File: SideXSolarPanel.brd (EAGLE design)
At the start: 81.7 x 102 mm, 33 parts

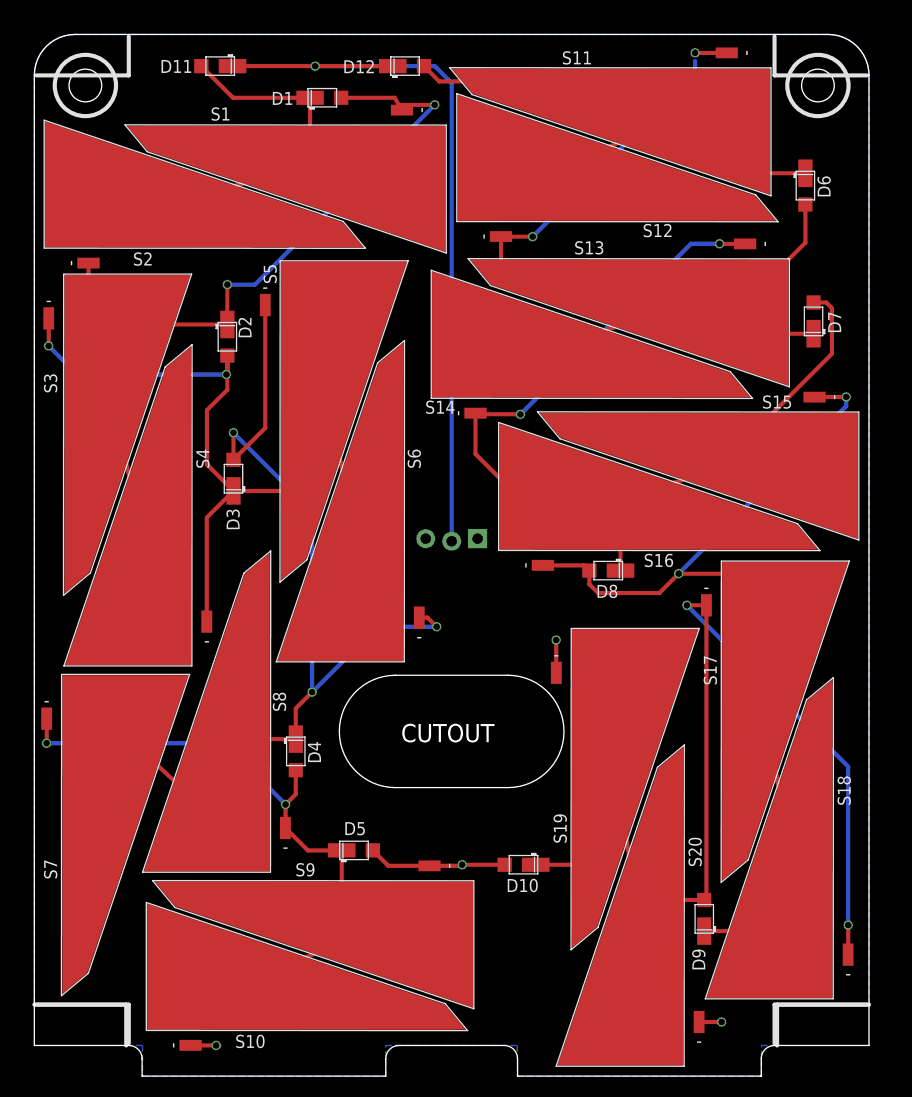
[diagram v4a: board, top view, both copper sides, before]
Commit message: Increased cutout line width
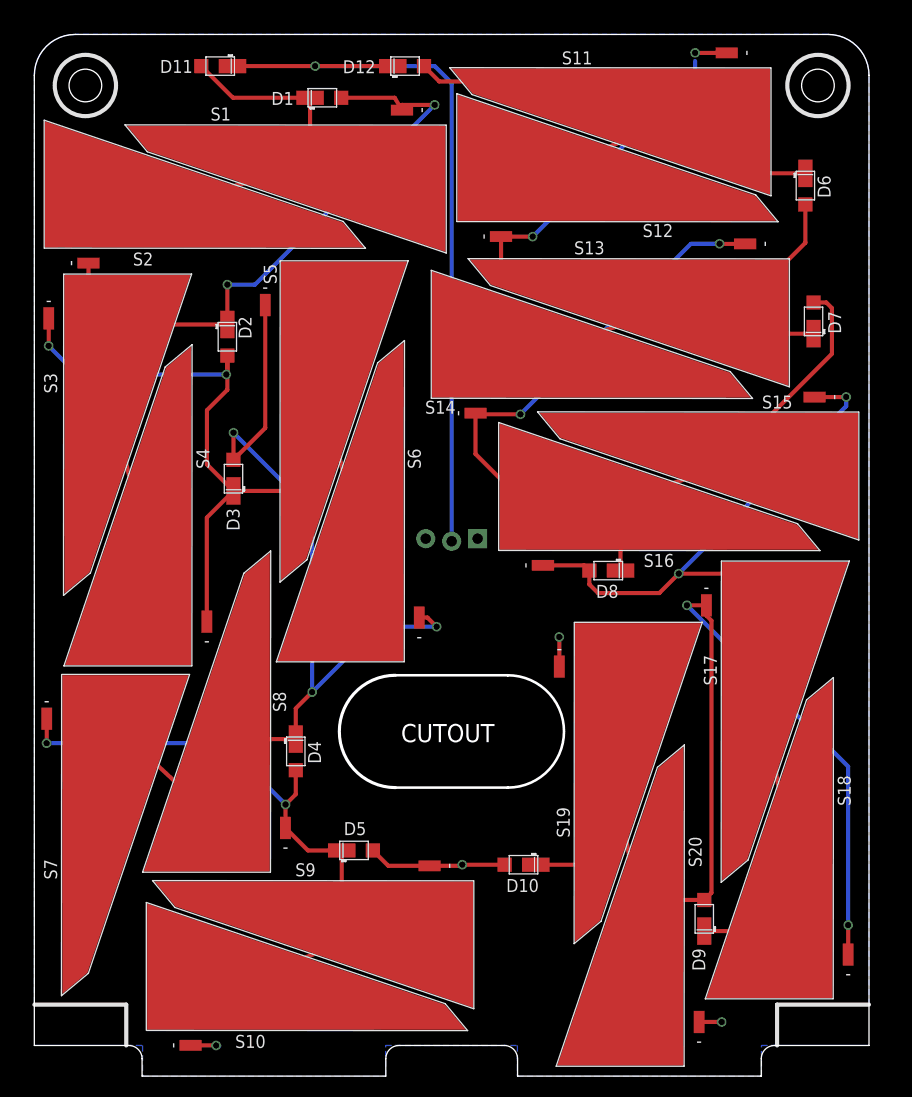
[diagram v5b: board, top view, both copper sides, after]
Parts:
- moved S19 0.67 mm to (53.0, 34.1)
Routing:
- net N$41: track 127.3 -> 128.2 mm
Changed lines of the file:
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@@
 <layer number="42" name="bRestrict" color="1" fill="10" visible="no" active="yes"/>
 <layer number="43" name="vRestrict" color="2" fill="10" visible="no" active="yes"/>
-<layer number="44" name="Drills" color="7" fill="1" visible="yes" active="yes"/>
-<layer number="45" name="Holes" color="7" fill="1" visible="yes" active="yes"/>
+<layer number="44" name="Drills" color="7" fill="1" visible="no" active="yes"/>
+<layer number="45" name="Holes" color="7" fill="1" visible="no" active="yes"/>
 <layer number="46" name="Milling" color="3" fill="1" visible="no" active="yes"/>
 <layer number="47" name="Measures" color="7" fill="1" visible="no" active="yes"/>
@@
 <wire x1="46.015" y1="0" x2="47.315" y2="-1.3" width="0" layer="20" curve="-90"/>
 <wire x1="71.18" y1="-1.3" x2="72.48" y2="0" width="0" layer="20" curve="-90"/>
-<wire x1="0.2" y1="4" x2="9.25" y2="4" width="0.4" layer="121"/>
-<wire x1="9.25" y1="4" x2="9.25" y2="0.2" width="0.4" layer="121"/>
-<wire x1="81.53" y1="94.99" x2="72.48" y2="94.99" width="0.4" layer="121"/>
-<wire x1="72.48" y1="94.99" x2="72.48" y2="98.79" width="0.4" layer="121"/>
-<wire x1="0.2" y1="94.99" x2="9.25" y2="94.99" width="0.4" layer="121"/>
-<wire x1="9.25" y1="94.99" x2="9.25" y2="98.79" width="0.4" layer="121"/>
-<wire x1="81.53" y1="4" x2="72.48" y2="4" width="0.4" layer="121"/>
-<wire x1="72.48" y1="4" x2="72.48" y2="0.2" width="0.4" layer="121"/>
-<rectangle x1="13.1" y1="58.8" x2="28.9" y2="77.8" layer="122"/>
 <hole x="5" y="94" drill="3.2"/>
 <hole x="76.73" y="94" drill="3.2"/>
-<wire x1="35.365" y1="25.25" x2="46.365" y2="25.25" width="0" layer="20"/>
-<wire x1="35.365" y1="36.25" x2="46.365" y2="36.25" width="0" layer="20"/>
-<wire x1="35.365" y1="36.25" x2="35.365" y2="25.25" width="0" layer="20" curve="180"/>
-<wire x1="46.365" y1="25.25" x2="46.365" y2="36.25" width="0" layer="20" curve="180"/>
+<wire x1="35.365" y1="25.25" x2="46.365" y2="25.25" width="0.254" layer="20"/>
+<wire x1="35.365" y1="36.25" x2="46.365" y2="36.25" width="0.254" layer="20"/>
+<wire x1="35.365" y1="36.25" x2="35.365" y2="25.25" width="0.3048" layer="20" curve="180"/>
+<wire x1="46.365" y1="25.25" x2="46.365" y2="36.25" width="0.254" layer="20" curve="180"/>
 <text x="35.9" y="29.7" size="1.778" layer="20">CUTOUT</text>
 <wire x1="0" y1="4" x2="9" y2="4" width="0.4064" layer="21"/>
@@
 <attribute name="NAME" x="9.65" y="76.37" size="1.27" layer="25"/>
 </element>
-<element name="S19" library="phonesat" package="SOLAR_CELL" value="SOLAR_CELL" x="52.7" y="33.5" smashed="yes">
-<attribute name="NAME" x="52.13" y="19.75" size="1.27" layer="25" rot="R90"/>
+<element name="S19" library="phonesat" package="SOLAR_CELL" value="SOLAR_CELL" x="53" y="34.1" smashed="yes">
+<attribute name="NAME" x="52.43" y="20.35" size="1.27" layer="25" rot="R90"/>
 </element>
 <element name="S20" library="phonesat" package="SOLAR_CELL" value="SOLAR_CELL" x="63.5" y="5.3" smashed="yes" rot="R180">
@@
 <wire x1="67.3" y1="2.3" x2="67.4" y2="2.3" width="0.4064" layer="16"/>
 <wire x1="67.4" y1="2.3" x2="67.4" y2="2.2" width="0.4064" layer="16"/>
-<wire x1="51.1107" y1="36.4991" x2="51.1" y2="36.4991" width="0.4064" layer="1"/>
-<wire x1="51.1" y1="36.4991" x2="51.1" y2="39.7" width="0.4064" layer="1"/>
-<via x="51.1" y="39.7" extent="1-16" drill="0.6"/>
-<wire x1="51.1" y1="39.7" x2="51.2" y2="39.7" width="0.4064" layer="16"/>
+<wire x1="51.4107" y1="37.0991" x2="51.1" y2="36.4991" width="0.4064" layer="1"/>
 <wire x1="38.6991" y1="17.5893" x2="34.6607" y2="17.5893" width="0.4064" layer="1"/>
 <wire x1="34.6607" y1="17.5893" x2="33.15" y2="19.1" width="0.4064" layer="1"/>
 <wire x1="46.05" y1="17.7" x2="41.9" y2="17.7" width="0.4064" layer="1"/>
+<wire x1="51.4107" y1="37.0991" x2="51.4107" y2="39.9893" width="0.4064" layer="1"/>
+<wire x1="51.4107" y1="39.9893" x2="51.4" y2="40" width="0.4064" layer="1"/>
+<via x="51.4" y="40" extent="1-16" drill="0.6"/>
+<wire x1="51.4" y1="40" x2="51.3" y2="40.1" width="0.4064" layer="16"/>
+<wire x1="51.3" y1="40.1" x2="43.405" y2="49.627" width="0" layer="19" extent="1-16"/>
 </signal>
 <signal name="N$36">
@@
 <contactref element="S17" pad="1"/>
 <contactref element="S19" pad="2"/>
-<wire x1="54.8874" y1="38.5114" x2="57.72385625" y2="21.63763125" width="0.4064" layer="1"/>
+<wire x1="55.1874" y1="39.1114" x2="57.72385625" y2="21.63763125" width="0.4064" layer="1"/>
 <wire x1="57.72385625" y1="21.63763125" x2="58.9777125" y2="14.178584375" width="0.4064" layer="1"/>
 <wire x1="58.9777125" y1="14.178584375" x2="61.3126" y2="0.2886" width="0.4064" layer="1"/>
@@
 <wire x1="65.6" y1="14.25" x2="59.049128125" y2="14.25" width="0.4064" layer="1"/>
 <wire x1="59.049128125" y1="14.25" x2="58.9777125" y2="14.178584375" width="0.4064" layer="1"/>
-<wire x1="65.8107" y1="43.0991" x2="65.8107" y2="14.4607" width="0.4064" layer="1"/>
-<wire x1="65.8107" y1="14.4607" x2="65.6" y2="14.25" width="0.4064" layer="1"/>
 <wire x1="79.6893" y1="8.9009" x2="79.6893" y2="11.7893" width="0.4064" layer="1"/>
 <wire x1="79.6893" y1="11.7893" x2="79.7" y2="11.8" width="0.4064" layer="1"/>
@@
 <wire x1="63.9" y1="43.1" x2="65.8098" y2="43.1" width="0.4064" layer="1"/>
 <wire x1="65.8098" y1="43.1" x2="65.8107" y2="43.0991" width="0.4064" layer="1"/>
+<wire x1="65.6" y1="14.25" x2="66.3" y2="14.95" width="0.4064" layer="1"/>
+<wire x1="66.3" y1="14.95" x2="66.3" y2="41.6" width="0.4064" layer="1"/>
+<wire x1="66.3" y1="41.6" x2="65.8107" y2="42.0893" width="0.4064" layer="1"/>
+<wire x1="65.8107" y1="42.0893" x2="65.8107" y2="43.0991" width="0.4064" layer="1"/>
 </signal>
 <signal name="N$45">

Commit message: Swapped X and Y solar panels per NanoRacks ICD
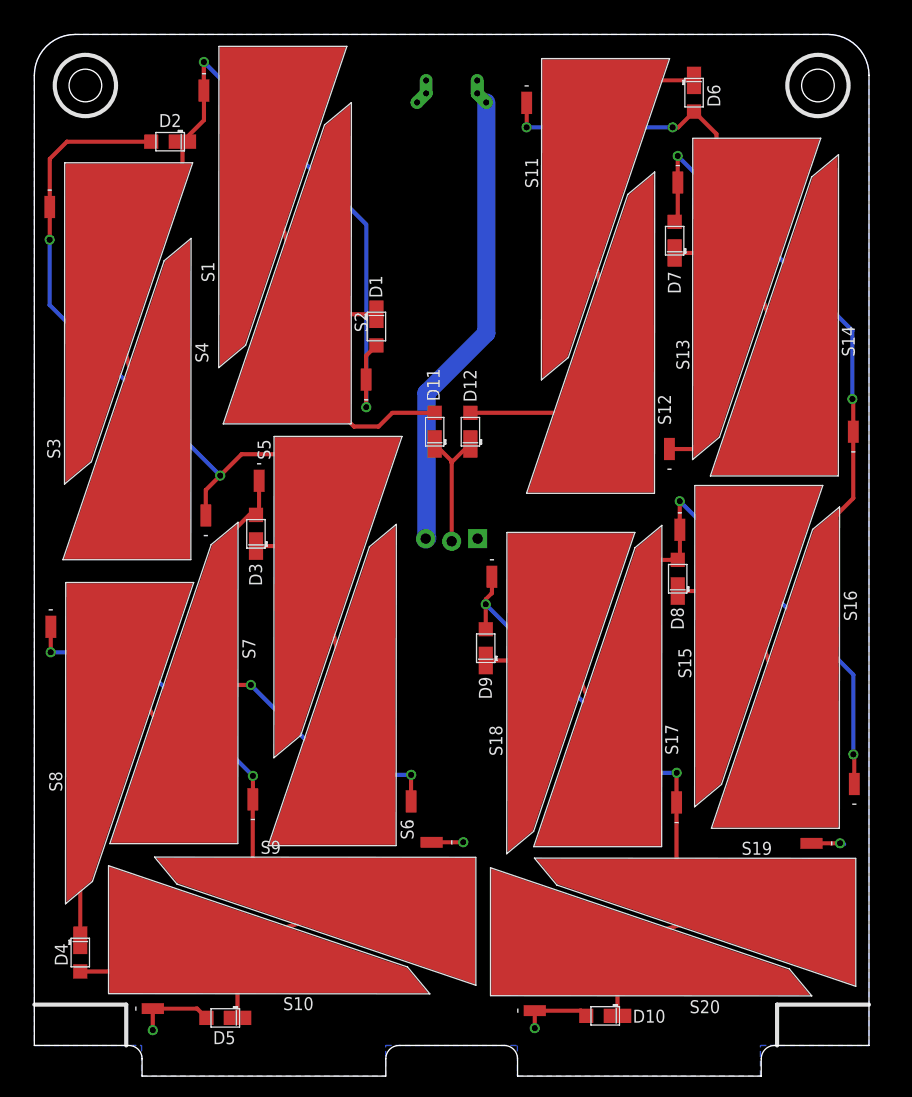
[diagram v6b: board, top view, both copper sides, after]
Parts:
- added U$1, U$2: BURNER, Burner:BURNER
- moved S18 44.3 mm to (46.4, 42.9), turned to 0 degrees
- moved D11 41.5 mm to (39.2, 60.1), turned to 90 degrees
- moved D12 36.4 mm to (42.7, 60.1), turned to 90 degrees
- moved D9 34.1 mm to (44.2, 38.9)
- moved S16 32.7 mm to (78.7, 28.6), turned to 180 degrees
- moved S14 32.4 mm to (78.6, 63.1), turned to 180 degrees
- moved D4 28.9 mm to (4.50, 9.10)
- moved S19 25.6 mm to (73.1, 18.2), turned to 270 degrees
- moved S2 24.7 mm to (30.9, 68.2), turned to 180 degrees
- moved S8 24.1 mm to (3.20, 38.0), turned to 0 degrees
- moved D1 23.0 mm to (33.5, 70.4), turned to 270 degrees
- moved S12 22.8 mm to (60.6, 61.4), turned to 180 degrees
- moved D5 20.7 mm to (18.7, 2.70), turned to 180 degrees
- moved D2 19.9 mm to (13.3, 88.5), turned to 180 degrees
- moved S6 18.0 mm to (35.3, 26.9)
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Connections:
- new net V_BURN: JP1.3, U$1.H1, U$1.H2, U$1.H3
- net GND: now also U$2.H1, U$2.H2, U$2.H3
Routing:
- net V_SOLAR: track 74.6 -> 12.8 mm, vias 1 -> 0
- net V_BURN: track 0.00 -> 45.2 mm
- net N$41: track 128.2 -> 86.1 mm
- net N$50: track 79.2 -> 96.5 mm
- net N$39: track 104.1 -> 119.4 mm, vias 3 -> 2
- net N$1: track 97.7 -> 86.0 mm
- net N$5: track 76.4 -> 66.1 mm
- net N$45: track 95.6 -> 103.4 mm
- net N$37: track 99.6 -> 103.9 mm
- net N$9: track 54.5 -> 53.3 mm
- net N$7: track 108.5 -> 107.4 mm
- net GND: track 22.9 -> 21.9 mm
- net N$36: track 98.5 -> 97.9 mm
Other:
- outline, holes or cut-outs redrawn
- board text removed: "CUTOUT"

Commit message: Cleanup
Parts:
- added FRAME1: FRAME-LETTER, SparkFun-Aesthetics:CREATIVE_COMMONS
- added U$3: KICKSAT_LOGO, KickSat-Logo:KICKSAT_LOGO
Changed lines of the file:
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@@
 <element name="U$1" library="Burner" package="BURNER" value="BURNER" x="43.365" y="94.5" rot="R270"/>
 <element name="U$2" library="Burner" package="BURNER" value="BURNER" x="38.365" y="94.5" rot="MR270"/>
+<element name="FRAME1" library="SparkFun-Aesthetics" package="CREATIVE_COMMONS" value="FRAME-LETTER" x="20.8" y="-10.6"/>
+<element name="U$3" library="KickSat-Logo" package="KICKSAT_LOGO" value="KICKSAT_LOGO" x="53.9" y="27.1" rot="MR0"/>
 </elements>
 <signals>

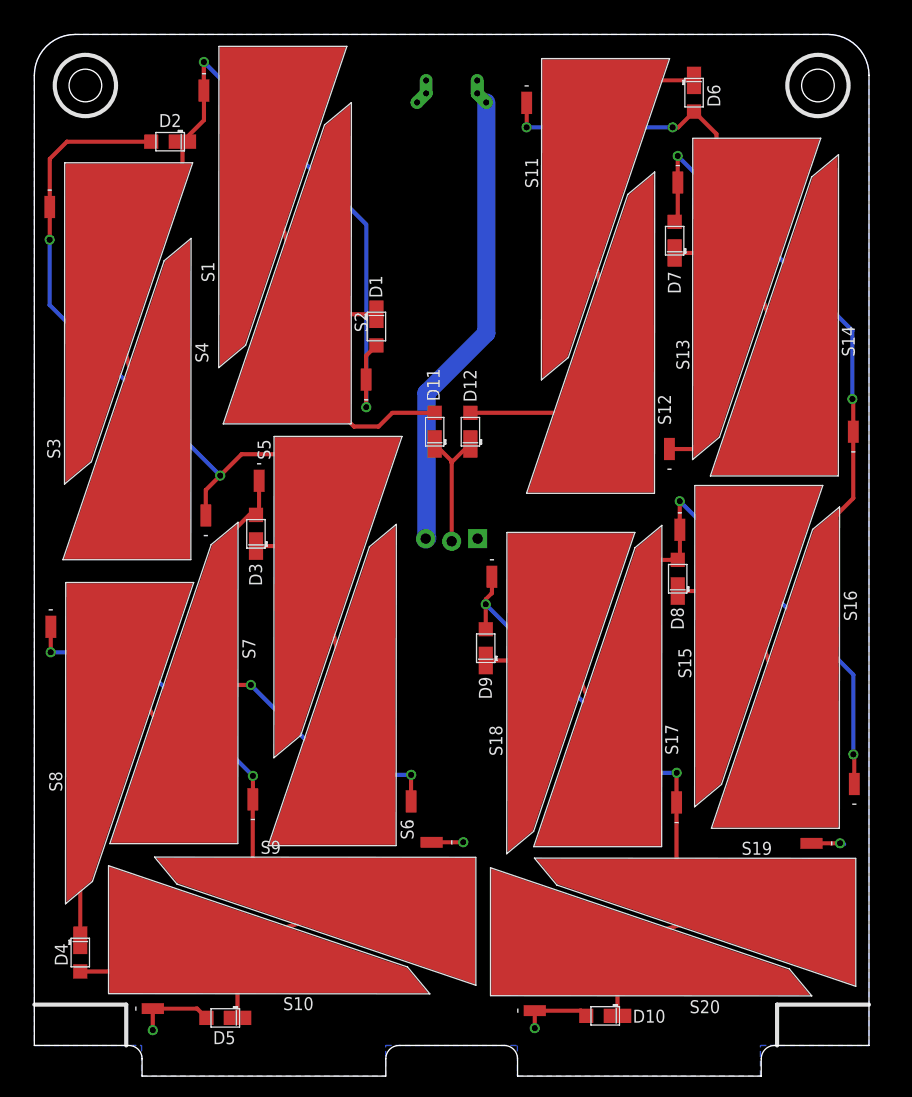
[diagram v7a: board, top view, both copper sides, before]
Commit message: Fixed solar cell footprints
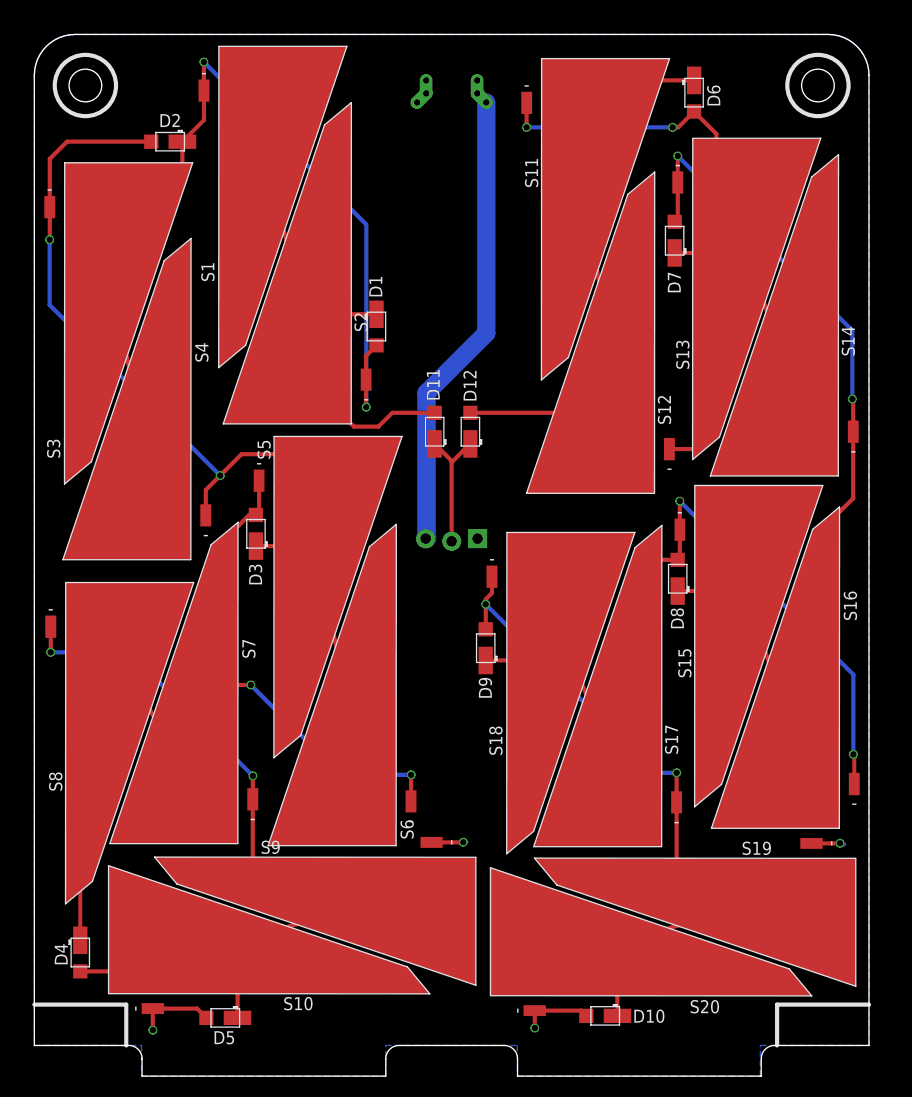
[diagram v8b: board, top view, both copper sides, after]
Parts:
- D1, D10, D11, D12, D2, D3, D4, D5, D6, D7, D8, D9: device phonesat:SB_DIODE -> Solar:SB_DIODE
- S1, S10, S11, S12, S13, S14, S15, S16, S17, S18, S19, S2, S20, S3, S4, S5, S6, S7, S8, S9: device phonesat:SOLAR_CELL -> Solar:SOLAR_CELL
